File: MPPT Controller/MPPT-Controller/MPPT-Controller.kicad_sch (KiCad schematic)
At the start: 46 parts, among them J1 Conn_01x02_Pin, J2 Conn_01x02_Pin, J3 Conn_01x02_Pin, J4 Conn_01x02_Pin, Q1 IRF540N, SW1 SW_SPDT, U1 ADS1115IDGS, U4 LM1117DT-3.3, U5 LM2596S-ADJ, U6 TC4422

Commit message: Update MPPT-Controller.kicad_sch
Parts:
- added C17: 470u, Capacitor_THT:C_Radial_D16.0mm_H25.0mm_P7.50mm, symbol Device:C
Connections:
- net VinterA: now also C17.1
- net at C16.2, D10.2 (A), Q1.1 (G)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: now also C17.2
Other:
- moved on the sheet: C16, D10, L2, Q1, R25

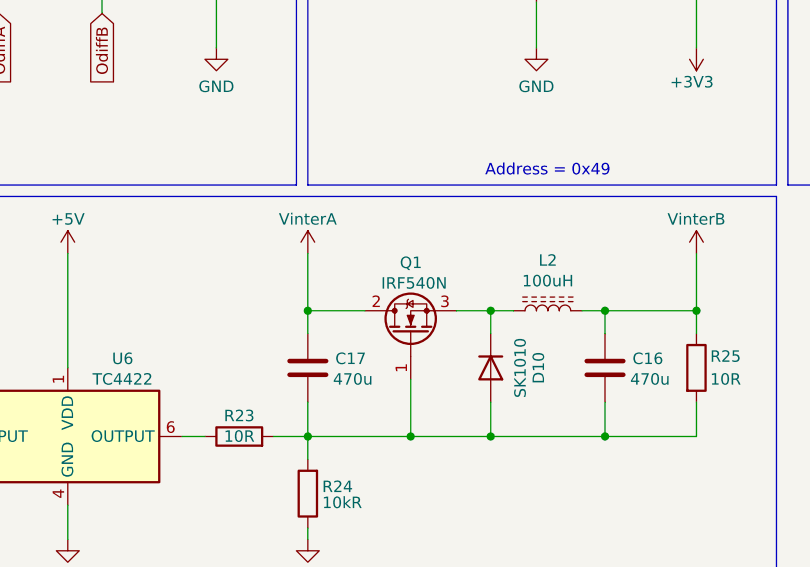
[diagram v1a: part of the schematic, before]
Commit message: Change to IRL Series
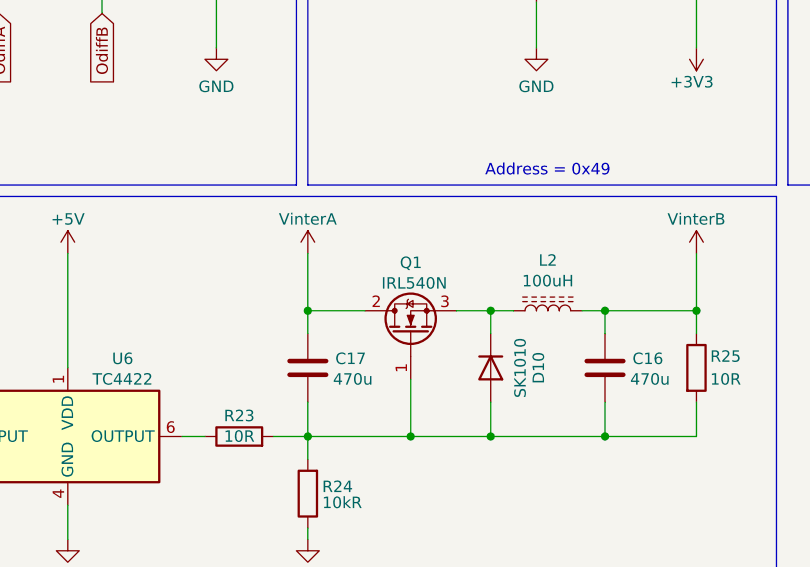
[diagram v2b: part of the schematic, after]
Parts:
- Q1: value IRF540N -> IRL540N
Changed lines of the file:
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@@
 			)
 		)
-		(property "Value" "IRF540N"
+		(property "Value" "IRL540N"
 			(at 133.604 82.042 90)
 			(effects

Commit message: Add footprints partial
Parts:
- F1, F2: footprint (none) -> Fuse:Fuseholder_Clip-5x20mm_Bel_FC-203-22_Lateral_P17.80x5.00mm_D1.17mm_Horizontal
- J1, J2, J3, J4: footprint (none) -> TerminalBlock:TerminalBlock_Altech_AK300-2_P5.00mm
- SW1: footprint (none) -> Button_Switch_SMD:SW_Push_1P1T_XKB_TS-1187A
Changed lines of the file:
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@@
 			)
 		)
-		(property "Footprint" ""
+		(property "Footprint" "Button_Switch_SMD:SW_Push_1P1T_XKB_TS-1187A"
 			(at 181.61 27.94 0)
 			(effects
@@
 			)
 		)
-		(property "Footprint" ""
+		(property "Footprint" "TerminalBlock:TerminalBlock_Altech_AK300-2_P5.00mm"
 			(at 20.32 90.17 0)
 			(effects
@@
 			)
 		)
-		(property "Footprint" ""
+		(property "Footprint" "TerminalBlock:TerminalBlock_Altech_AK300-2_P5.00mm"
 			(at 20.32 118.11 0)
 			(effects
@@
 			)
 		)
-		(property "Footprint" ""
+		(property "Footprint" "TerminalBlock:TerminalBlock_Altech_AK300-2_P5.00mm"
 			(at 52.07 135.89 0)
 			(effects
@@
 			)
 		)
-		(property "Footprint" ""
+		(property "Footprint" "Fuse:Fuseholder_Clip-5x20mm_Bel_FC-203-22_Lateral_P17.80x5.00mm_D1.17mm_Horizontal"
 			(at 183.388 39.37 90)
 			(effects
@@
 			)
 		)
-		(property "Footprint" ""
+		(property "Footprint" "TerminalBlock:TerminalBlock_Altech_AK300-2_P5.00mm"
 			(at 59.69 90.17 0)
 			(effects
@@
 			)
 		)
-		(property "Footprint" ""
+		(property "Footprint" "Fuse:Fuseholder_Clip-5x20mm_Bel_FC-203-22_Lateral_P17.80x5.00mm_D1.17mm_Horizontal"
 			(at 29.718 85.09 90)
 			(effects

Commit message: Apply Footprints
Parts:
- L2: footprint (none) -> Inductor_THT:L_Toroid_Vertical_L25.4mm_W14.7mm_P12.20mm_Vishay_TJ5_BigPads
- LR1, LR2, LR3, LR4: footprint (none) -> Resistor_SMD:R_4020_10251Metric
- R2, R3, R4, R5, R7, R8: footprint (none) -> Resistor_SMD:R_0603_1608Metric_Pad0.98x0.95mm_HandSolder
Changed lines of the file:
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@@
 			)
 		)
-		(property "Footprint" ""
+		(property "Footprint" "Inductor_THT:L_Toroid_Vertical_L25.4mm_W14.7mm_P12.20mm_Vishay_TJ5_BigPads"
 			(at 144.78 85.09 0)
 			(effects
@@
 			)
 		)
-		(property "Footprint" ""
+		(property "Footprint" "Resistor_SMD:R_0603_1608Metric_Pad0.98x0.95mm_HandSolder"
 			(at 29.972 45.72 90)
 			(effects
@@
 			)
 		)
-		(property "Footprint" ""
+		(property "Footprint" "Resistor_SMD:R_4020_10251Metric"
 			(at 81.28 33.528 90)
 			(effects
@@
 			)
 		)
-		(property "Footprint" ""
+		(property "Footprint" "Resistor_SMD:R_4020_10251Metric"
 			(at 46.99 33.528 90)
 			(effects
@@
 			)
 		)
-		(property "Footprint" ""
+		(property "Footprint" "Resistor_SMD:R_0603_1608Metric_Pad0.98x0.95mm_HandSolder"
 			(at 82.042 45.72 90)
 			(effects
@@
 			)
 		)
-		(property "Footprint" ""
+		(property "Footprint" "Resistor_SMD:R_0603_1608Metric_Pad0.98x0.95mm_HandSolder"
 			(at 93.472 45.72 90)
 			(effects
@@
 			)
 		)
-		(property "Footprint" ""
+		(property "Footprint" "Resistor_SMD:R_0603_1608Metric_Pad0.98x0.95mm_HandSolder"
 			(at 41.402 45.72 90)
 			(effects
@@
 			)
 		)
-		(property "Footprint" ""
+		(property "Footprint" "Resistor_SMD:R_0603_1608Metric_Pad0.98x0.95mm_HandSolder"
 			(at 41.402 143.51 90)
 			(effects
@@
 			)
 		)
-		(property "Footprint" ""
+		(property "Footprint" "Resistor_SMD:R_4020_10251Metric"
 			(at 99.06 33.528 90)
 			(effects
@@
 			)
 		)
-		(property "Footprint" ""
+		(property "Footprint" "Resistor_SMD:R_4020_10251Metric"
 			(at 29.21 33.528 90)
 			(effects
@@
 			)
 		)
-		(property "Footprint" ""
+		(property "Footprint" "Resistor_SMD:R_0603_1608Metric_Pad0.98x0.95mm_HandSolder"
 			(at 29.972 143.51 90)
 			(effects

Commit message: Create ~MPPT-Controller.kicad_pcb.lck
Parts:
- SW1: footprint Button_Switch_SMD:SW_Push_1P1T_XKB_TS-1187A -> Connector_PinHeader_2.54mm:PinHeader_1x03_P2.54mm_Vertical
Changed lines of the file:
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@@
 			)
 		)
-		(property "Footprint" "Button_Switch_SMD:SW_Push_1P1T_XKB_TS-1187A"
+		(property "Footprint" "Connector_PinHeader_2.54mm:PinHeader_1x03_P2.54mm_Vertical"
 			(at 181.61 27.94 0)
 			(effects

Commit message: Add 2nd Power Measure
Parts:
- added U7: ADS1115IDGS, Package_SO:TSSOP-10_3x3mm_P0.5mm, symbol Analog_ADC:ADS1115IDGS
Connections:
- net +3V3: now also U7.8 (VDD)
- net GND: now also U7.1 (ADDR), U7.3 (GND)
- net IdiffA: now also U7.4 (AIN0)
- net IdiffB: now also U7.5 (AIN1)
- net SCL: now also U7.10 (SCL)
- net SDA: now also U7.9 (SDA)
- net VoltIn: now also U7.6 (AIN2)
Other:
- note added: "Address = 0x??"
- moved on the sheet: C13, C14, C15, C16, C17, D10, D7, D8, F2, L1, L2, Q1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

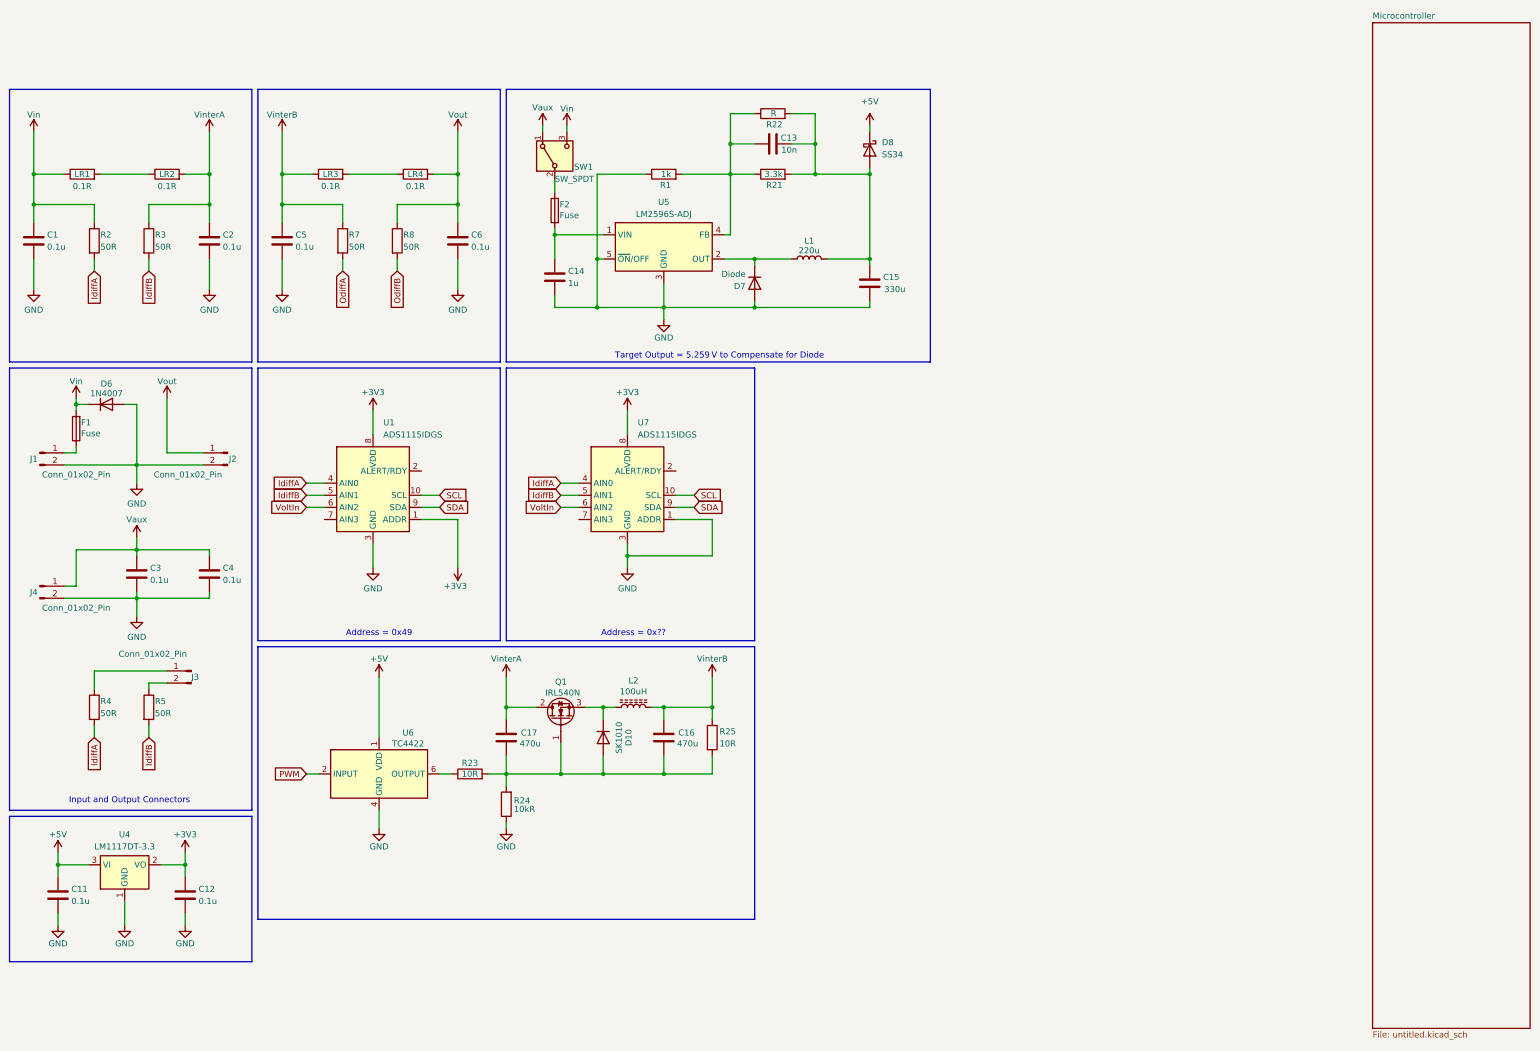
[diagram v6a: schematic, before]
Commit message: Add Bypass Supply for FET Driver
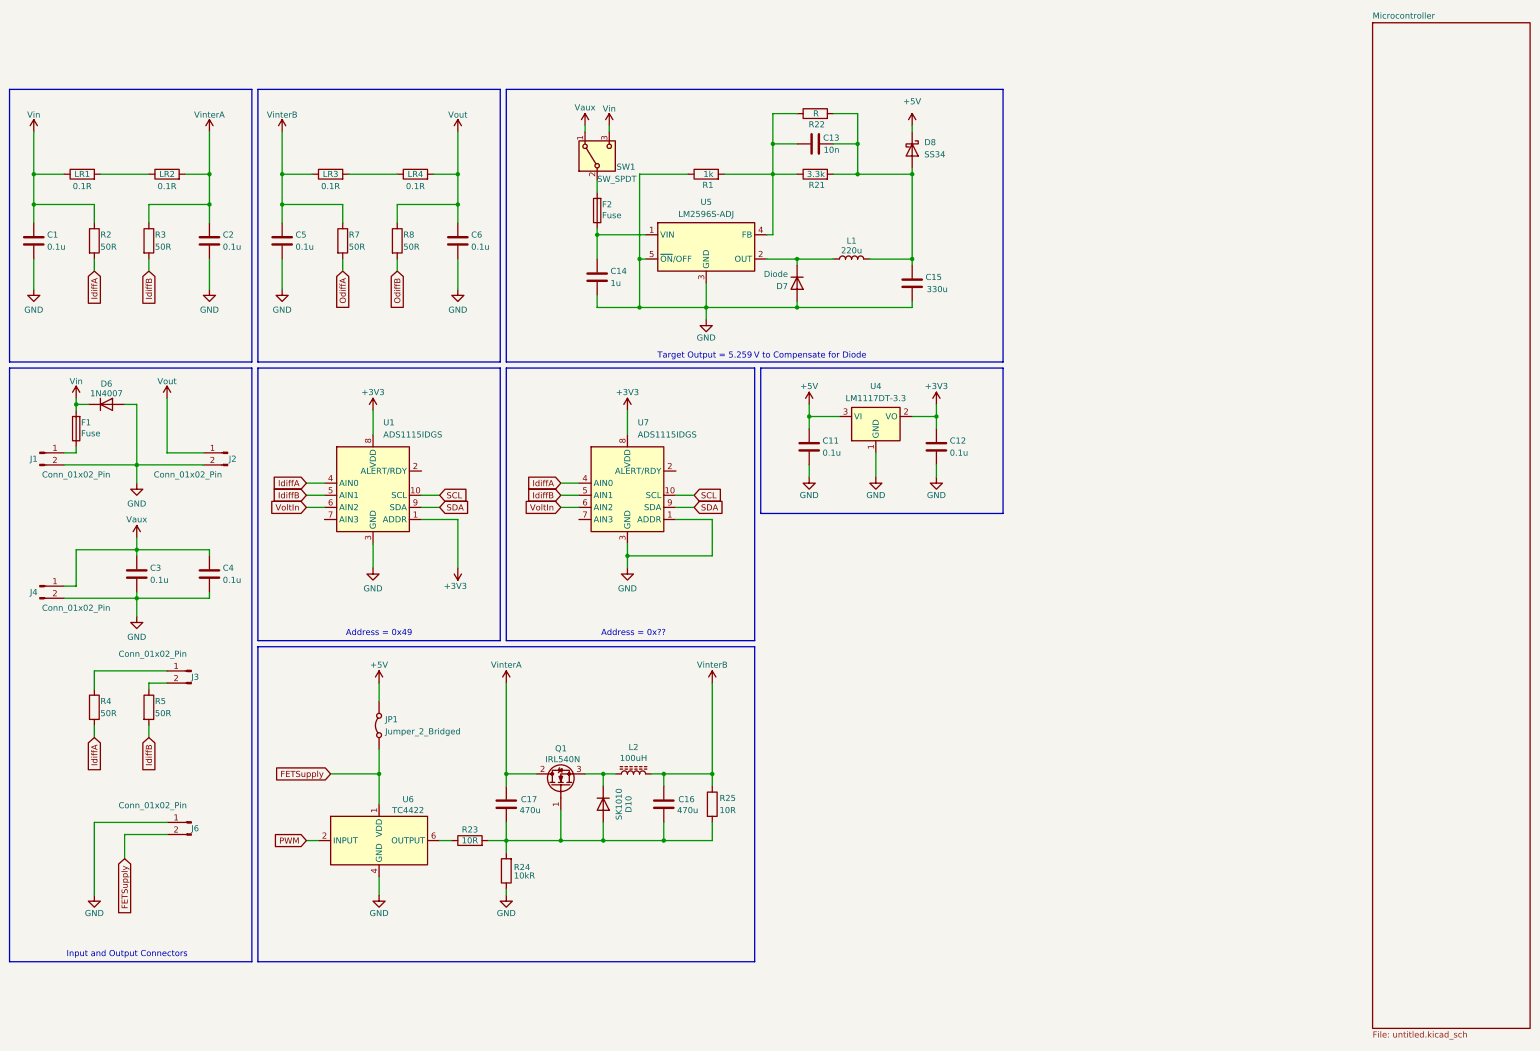
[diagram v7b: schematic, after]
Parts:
- added J6: Conn_01x02_Pin, TerminalBlock:TerminalBlock_Altech_AK300-2_P5.00mm, symbol Connector:Conn_01x02_Pin
- added JP1: Jumper_2_Bridged, TestPoint:TestPoint_2Pads_Pitch2.54mm_Drill0.8mm, symbol Jumper:Jumper_2_Bridged
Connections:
- net +5V: now also JP1.2 (B); no longer U6.1 (VDD), U6.8 (VDD)
- net GND: now also J6.1 (Pin_1)
- new net FETSupply: J6.2 (Pin_2), JP1.1 (A), U6.1 (VDD), U6.8 (VDD)
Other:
- moved on the sheet: C11, C12, C13, C14, C15, C16, C17, D10, D7, D8, F2, L1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
